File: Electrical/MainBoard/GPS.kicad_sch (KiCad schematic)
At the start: 4 parts, among them J24 Conn_01x04, U14 MAX-M8C-0

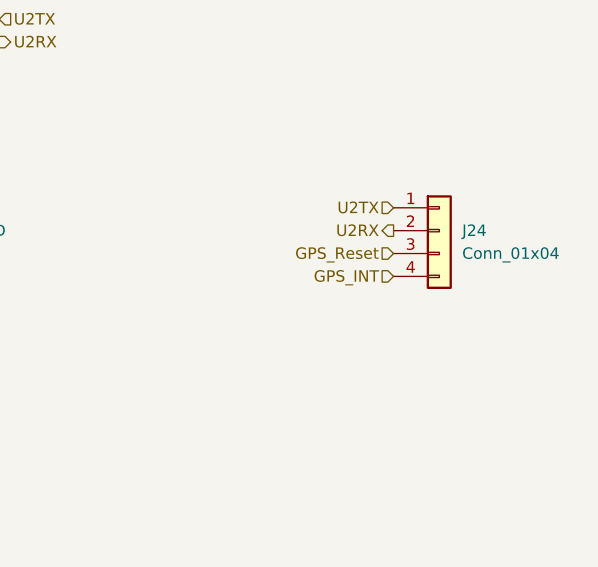
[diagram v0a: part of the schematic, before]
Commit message: Change some connections to picoblade, add env sensor connector
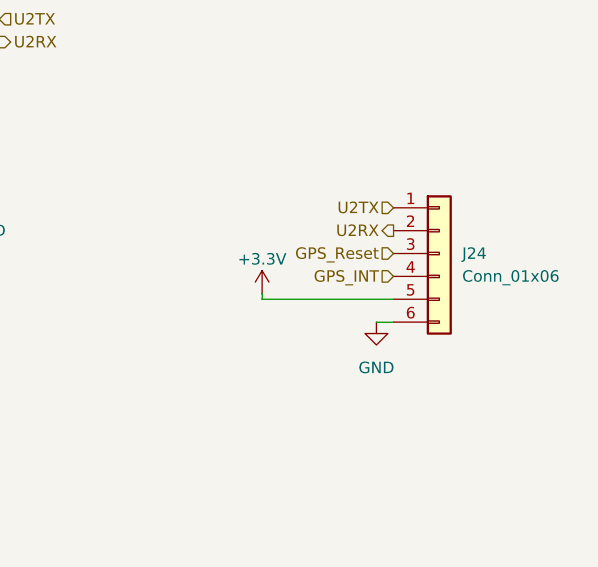
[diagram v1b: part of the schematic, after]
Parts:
- removed J24: Conn_01x04, RobotLibrary:CONN_22-23-2041_MOL, symbol Connector_Generic:Conn_01x04
- added J24: Conn_01x06, Connector_Molex:Molex_PicoBlade_53047-0610_1x06_P1.25mm_Vertical, symbol Connector_Generic:Conn_01x06
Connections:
- net +3.3V: now also J24.5 (Pin_5)
- net GND: now also J24.6 (Pin_6)
- net GPS_INT: now also J24.4 (Pin_4)
- net GPS_Reset: now also J24.3 (Pin_3)
- net U2RX: now also J24.2 (Pin_2)
- net U2TX: now also J24.1 (Pin_1)
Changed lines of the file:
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@@
 	(title_block
 		(title "MCU Controller")
-		(rev "0.3")
+		(date "2025-08-06")
+		(rev "0.4")
 		(company "satomm@stanford.edu")
 		(comment 1 "Department of Civil and Environmental Engineering")
@@
 	(wire
 		(pts
+			(xy 199.39 132.08) (xy 184.785 132.08)
+		)
+		(stroke
+			(width 0)
+			(type default)
+		)
+	)
+	(wire
+		(pts
 			(xy 158.75 182.88) (xy 161.925 182.88)
 		)
@@
 	(wire
 		(pts
+			(xy 184.785 132.08) (xy 184.785 131.445)
+		)
+		(stroke
+			(width 0)
+			(type default)
+		)
+	)
+	(wire
+		(pts
 			(xy 155.575 80.645) (xy 155.575 78.105)
 		)
@@
 		(pts
 			(xy 154.305 119.38) (xy 154.305 118.745)
+		)
+		(stroke
+			(width 0)
+			(type default)
+		)
+	)
+	(wire
+		(pts
+			(xy 197.485 134.62) (xy 199.39 134.62)
 		)
 		(stroke
@@
 	)
 	(symbol
-		(lib_id "Connector_Generic:Conn_01x04")
-		(at 204.47 124.46 0)
-		(unit 1)
-		(exclude_from_sim no)
-		(in_bom no)
-		(on_board yes)
-		(dnp no)
-		(fields_autoplaced yes)
-		(property "Reference" "J24"
-			(at 207.01 124.46 0)
-			(effects
-				(font
-					(size 1.27 1.27)
-				)
-				(justify left)
-			)
-		)
-		(property "Value" "Conn_01x04"
-			(at 207.01 127 0)
-			(effects
-				(font
-					(size 1.27 1.27)
-				)
-				(justify left)
-			)
-		)
-		(property "Footprint" "RobotLibrary:CONN_22-23-2041_MOL"
-			(at 204.47 124.46 0)
-			(effects
-				(font
-					(size 1.27 1.27)
-				)
-				(hide yes)
-			)
-		)
-		(property "Datasheet" "~"
-			(at 204.47 124.46 0)
-			(effects
-				(font
-					(size 1.27 1.27)
-				)
-				(hide yes)
-			)
-		)
-		(property "Description" ""
-			(at 204.47 124.46 0)
-			(effects
-				(font
-					(size 1.27 1.27)
-				)
-				(hide yes)
-			)
-		)
-		(property "Mfr" "Molex"
-			(at 204.47 124.46 0)
-			(effects
-				(font
-					(size 1.27 1.27)
-				)
-				(hide yes)
-			)
-		)
-		(property "Mfr P/N" "0022232041"
-			(at 204.47 124.46 0)
-			(effects
-				(font
-					(size 1.27 1.27)
-				)
-				(hide yes)
-			)
-		)
-		(property "Supplier 1" "DigiKey"
-			(at 204.47 124.46 0)
-			(effects
-				(font
-					(size 1.27 1.27)
-				)
-				(hide yes)
-			)
-		)
-		(property "Supplier 1 P/N" "WM4202-ND"
-			(at 204.47 124.46 0)
-			(effects
-				(font
-					(size 1.27 1.27)
-				)
-				(hide yes)
-			)
-		)
-		(property "Supplier 2" ""
-			(at 204.47 124.46 0)
-			(effects
-				(font
-					(size 1.27 1.27)
-				)
-				(hide yes)
-			)
-		)
-		(property "Supplier 2 P/N" ""
-			(at 204.47 124.46 0)
-			(effects
-				(font
-					(size 1.27 1.27)
-				)
-				(hide yes)
-			)
-		)
-		(pin "1"
-		)
-		(pin "2"
-		)
-		(pin "3"
-		)
-		(pin "4"
-		)
-		(instances
-			(project "MainBoard"
-				(path "/bd24c4db-4e36-4117-bd4f-5228ef241da9/3efd4746-229a-4377-9033-64e7155c364f"
-					(reference "J24")
-					(unit 1)
-				)
-			)
-		)
-	)
-	(symbol
 		(lib_id "RobotLibary:MAX-M8C-0")
 		(at 128.27 95.885 0)
@@
 				(path "/bd24c4db-4e36-4117-bd4f-5228ef241da9/3efd4746-229a-4377-9033-64e7155c364f"
 					(reference "C34")
+					(unit 1)
+				)
+			)
+		)
+	)
+	(symbol
+		(lib_id "power:GND")
+		(at 197.485 134.62 0)
+		(unit 1)
+		(exclude_from_sim no)
+		(in_bom yes)
+		(on_board yes)
+		(dnp no)
+		(fields_autoplaced yes)
+		(property "Reference" "#PWR051"
+			(at 197.485 140.97 0)
+			(effects
+				(font
+					(size 1.27 1.27)
+				)
+				(hide yes)
+			)
+		)
+		(property "Value" "GND"
+			(at 197.485 139.7 0)
+			(effects
+				(font
+					(size 1.27 1.27)
+				)
+			)
+		)
+		(property "Footprint" ""
+			(at 197.485 134.62 0)
+			(effects
+				(font
+					(size 1.27 1.27)
+				)
+				(hide yes)
+			)
+		)
+		(property "Datasheet" ""
+			(at 197.485 134.62 0)
+			(effects
+				(font
+					(size 1.27 1.27)
+				)
+				(hide yes)
+			)
+		)
+		(property "Description" ""
+			(at 197.485 134.62 0)
+			(effects
+				(font
+					(size 1.27 1.27)
+				)
+			)
+		)
+		(pin "1"
+		)
+		(instances
+			(project "MainBoard"
+				(path "/bd24c4db-4e36-4117-bd4f-5228ef241da9/3efd4746-229a-4377-9033-64e7155c364f"
+					(reference "#PWR051")
 					(unit 1)
 				)
@@
 	)
 	(symbol
+		(lib_id "power:+3.3V")
+		(at 184.785 131.445 0)
+		(unit 1)
+		(exclude_from_sim no)
+		(in_bom yes)
+		(on_board yes)
+		(dnp no)
+		(property "Reference" "#PWR050"
+			(at 184.785 135.255 0)
+			(effects
+				(font
+					(size 1.27 1.27)
+				)
+				(hide yes)
+			)
+		)
+		(property "Value" "+3.3V"
+			(at 184.785 127.635 0)
+			(effects
+				(font
+					(size 1.27 1.27)
+				)
+			)
+		)
+		(property "Footprint" ""
+			(at 184.785 131.445 0)
+			(effects
+				(font
+					(size 1.27 1.27)
+				)
+				(hide yes)
+			)
+		)
+		(property "Datasheet" ""
+			(at 184.785 131.445 0)
+			(effects
+				(font
+					(size 1.27 1.27)
+				)
+				(hide yes)
+			)
+		)
+		(property "Description" ""
+			(at 184.785 131.445 0)
+			(effects
+				(font
+					(size 1.27 1.27)
+				)
+			)
+		)
+		(pin "1"
+		)
+		(instances
+			(project "MainBoard"
+				(path "/bd24c4db-4e36-4117-bd4f-5228ef241da9/3efd4746-229a-4377-9033-64e7155c364f"
+					(reference "#PWR050")
+					(unit 1)
+				)
+			)
+		)
+	)
+	(symbol
 		(lib_id "RobotLibary:APAE1590R2540AKDB1-T")
 		(at 79.375 86.36 0)
@@
 					(unit 1)
 				)
+			)
+		)
+	)
+	(symbol
+		(lib_id "Connector_Generic:Conn_01x06")
+		(at 204.47 127 0)
+		(unit 1)
+		(exclude_from_sim no)
+		(in_bom yes)
+		(on_board yes)
+		(dnp no)
+		(property "Reference" "J24"
+			(at 207.01 126.9999 0)
+			(effects
+				(font
+					(size 1.27 1.27)
+				)
+				(justify left)
+			)
+		)
+		(property "Value" "Conn_01x06"
+			(at 207.01 129.5399 0)
+			(effects
+				(font
+					(size 1.27 1.27)
+				)
+				(justify left)
+			)
+		)
+		(property "Footprint" "Connector_Molex:Molex_PicoBlade_53047-0610_1x06_P1.25mm_Vertical"
+			(at 204.47 127 0)
+			(effects
+				(font
+					(size 1.27 1.27)
+				)
+				(hide yes)
+			)
+		)
+		(property "Datasheet" "https://www.molex.com/pdm_docs/sd/530470610_sd.pdf"
+			(at 204.47 127 0)
+			(effects
+				(font
+					(size 1.27 1.27)
+				)
+				(hide yes)
+			)
+		)
+		(property "Description" "Generic connector, single row, 01x06, script generated (kicad-library-utils/schlib/autogen/connector/)"
+			(at 204.47 127 0)
+			(effects
+				(font
+					(size 1.27 1.27)
+				)
+				(hide yes)
+			)
+		)
+		(property "Mfr" "Molex"
+			(at 204.47 127 0)
+			(effects
+				(font
+					(size 1.27 1.27)
+				)
+				(hide yes)
+			)
+		)
+		(property "Mfr P/N" "0530470610"
+			(at 204.47 127 0)
+			(effects
+				(font
+					(size 1.27 1.27)
+				)
+				(hide yes)
+			)
+		)
+		(property "Supplier 1" "DigiKey"
+			(at 204.47 127 0)
+			(effects
+				(font
+					(size 1.27 1.27)
+				)
+				(hide yes)
+			)
+		)
+		(property "Supplier 1 P/N" "WM1735-ND"
+			(at 204.47 127 0)
+			(effects
+				(font
+					(size 1.27 1.27)
+				)
+				(hide yes)
+			)
+		)
+		(property "Supplier 2" ""
+			(at 204.47 127 0)
+			(effects
+				(font
+					(size 1.27 1.27)
+				)
+				(hide yes)
+			)
+		)
+		(property "Supplier 2 P/N" ""
+			(at 204.47 127 0)
+			(effects
+				(font
+					(size 1.27 1.27)
+				)
+				(hide yes)
+			)
+		)
+		(pin "4"
+		)
+		(pin "2"
+		)
+		(pin "1"
+		)
+		(pin "3"
+		)
+		(pin "6"
+		)
+		(pin "5"
+		)
+		(instances
+			(project "MainBoard"
+				(path "/bd24c4db-4e36-4117-bd4f-5228ef241da9/3efd4746-229a-4377-9033-64e7155c364f"
+					(reference "J24")
+					(unit 1)
+				)

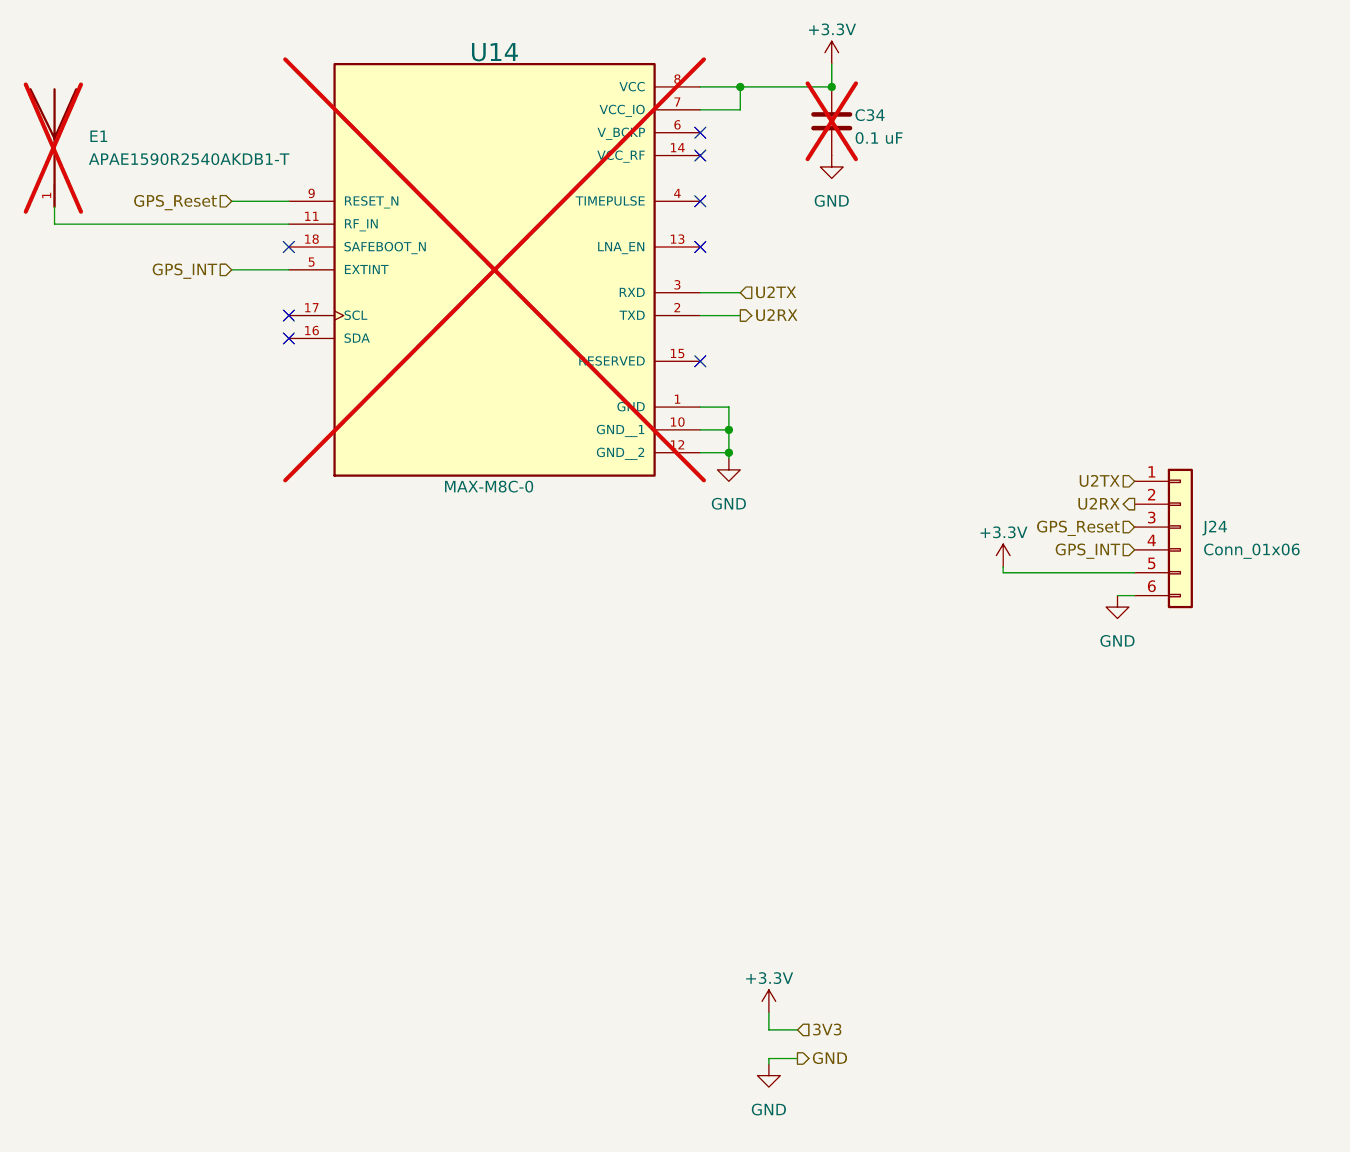
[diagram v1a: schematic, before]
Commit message: Use more molex picoblades and make schematic prettier
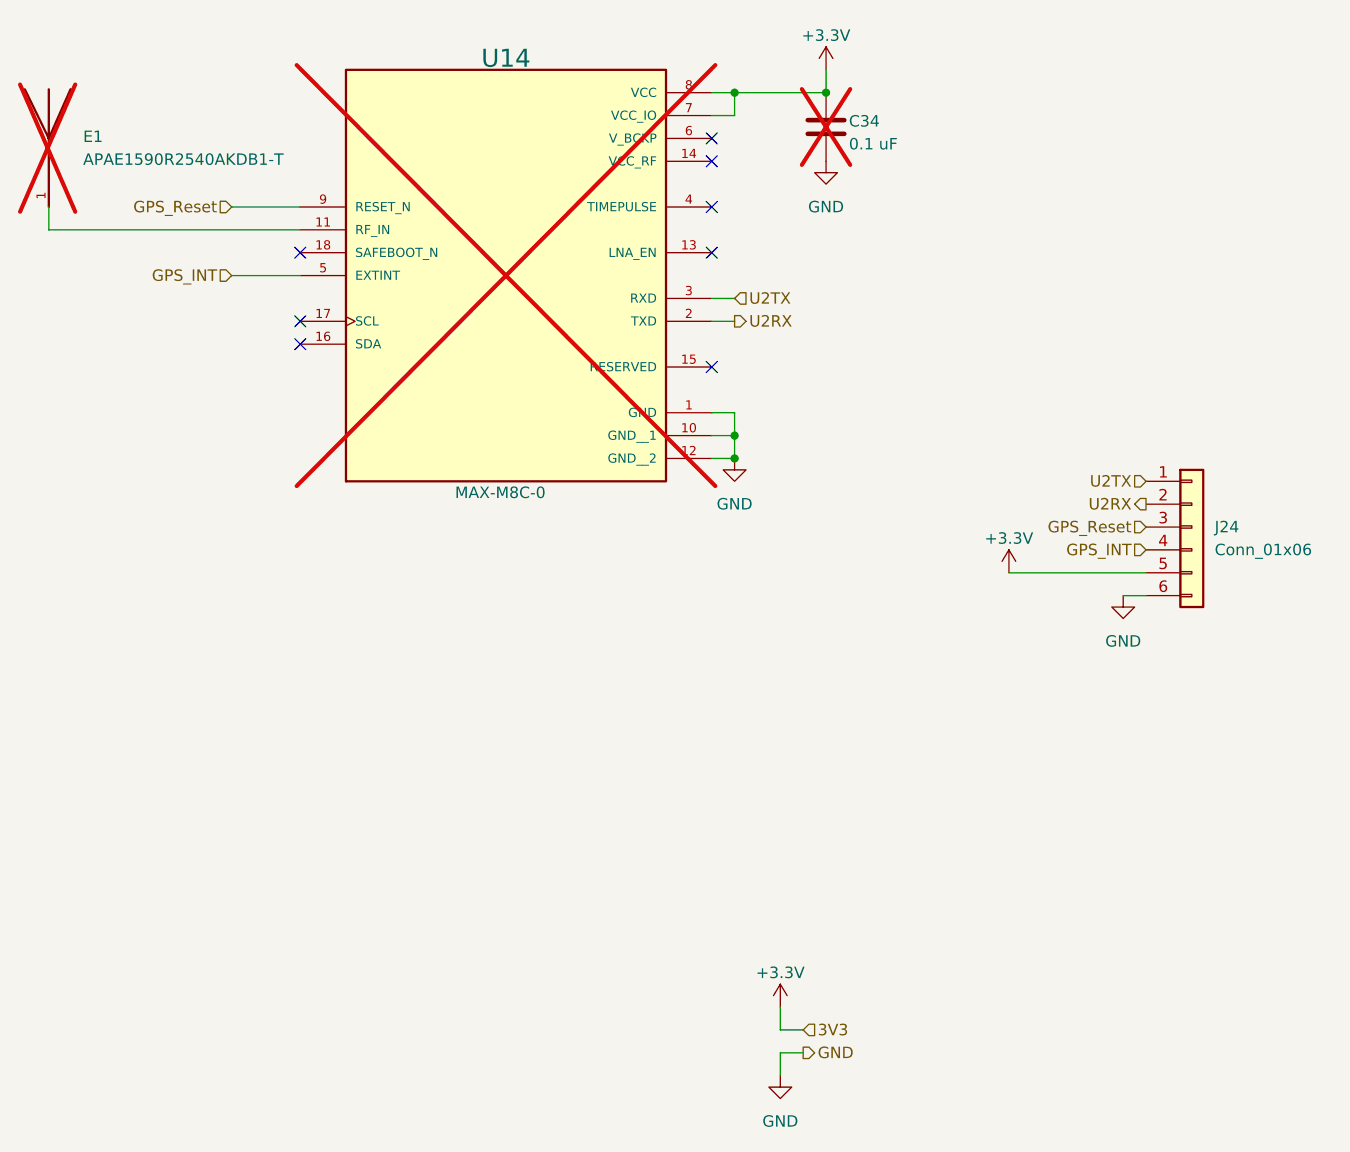
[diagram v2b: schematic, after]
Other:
- moved on the sheet: C34, E1, J24, U14

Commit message: Finalize updated schematics
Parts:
- J24: now left out of the parts list
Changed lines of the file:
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@@
 		(unit 1)
 		(exclude_from_sim no)
-		(in_bom yes)
+		(in_bom no)
 		(on_board yes)
 		(dnp no)
